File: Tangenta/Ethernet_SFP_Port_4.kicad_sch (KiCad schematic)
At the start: 2 parts, among them J9 HC-SFP-01L

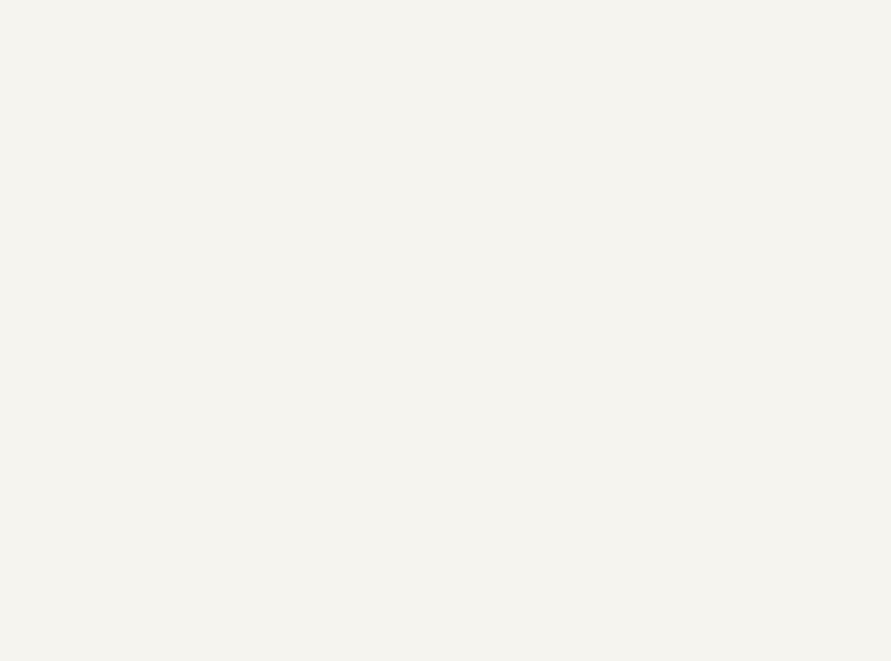
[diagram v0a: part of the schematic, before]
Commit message: Ethernet Switch schematic done, ports TBD...
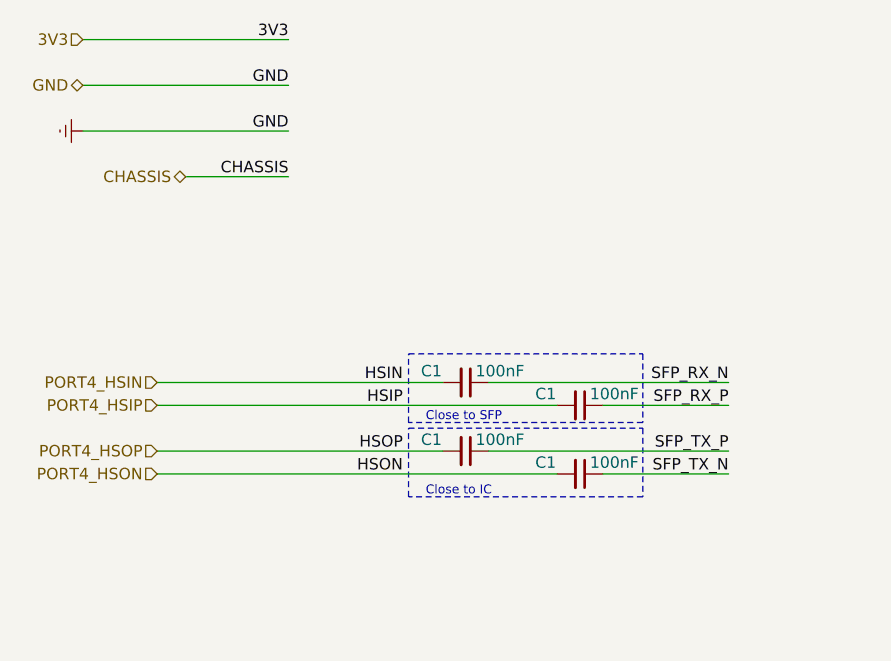
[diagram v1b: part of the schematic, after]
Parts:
- added C1 (x4): 100nF, Capacitor_SMD:C_0402_1005Metric, symbol Device:C_Small
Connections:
- new net PORT4_HSIN: C1.2
- new net PORT4_HSIP: C1.2
- new net PORT4_HSON: C1.2
- new net PORT4_HSOP: C1.2
- new net SFP_RX_N: C1.1
- new net SFP_RX_P: C1.1
- new net SFP_TX_N: C1.1
- new net SFP_TX_P: C1.1
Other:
- note added: "Close to IC"
- note added: "Close to SFP"

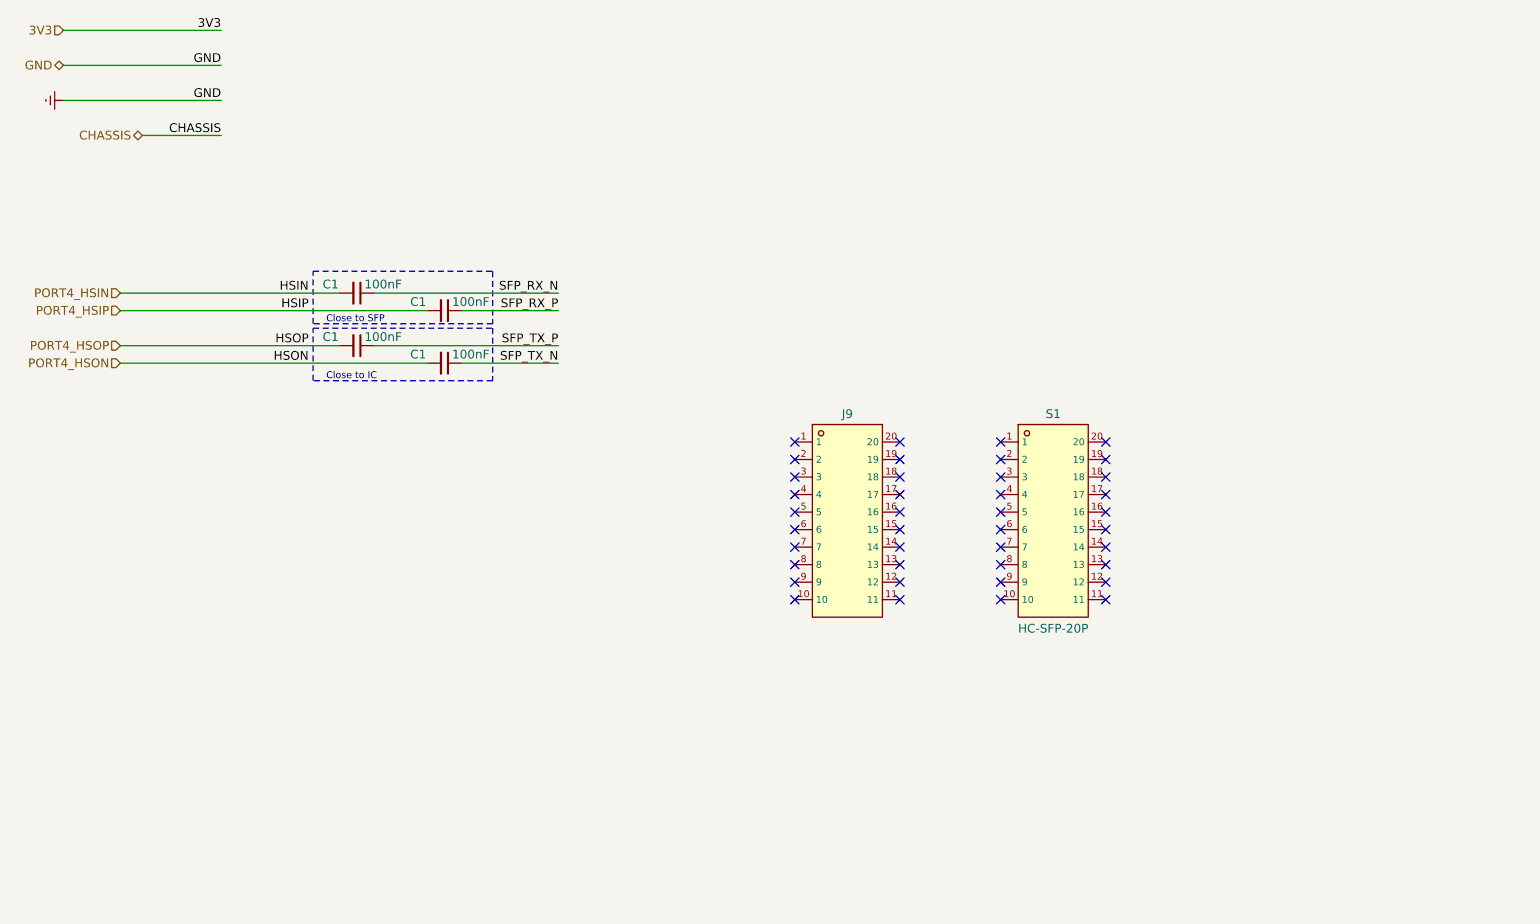
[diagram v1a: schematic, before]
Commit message: Ethernet ready for routing.
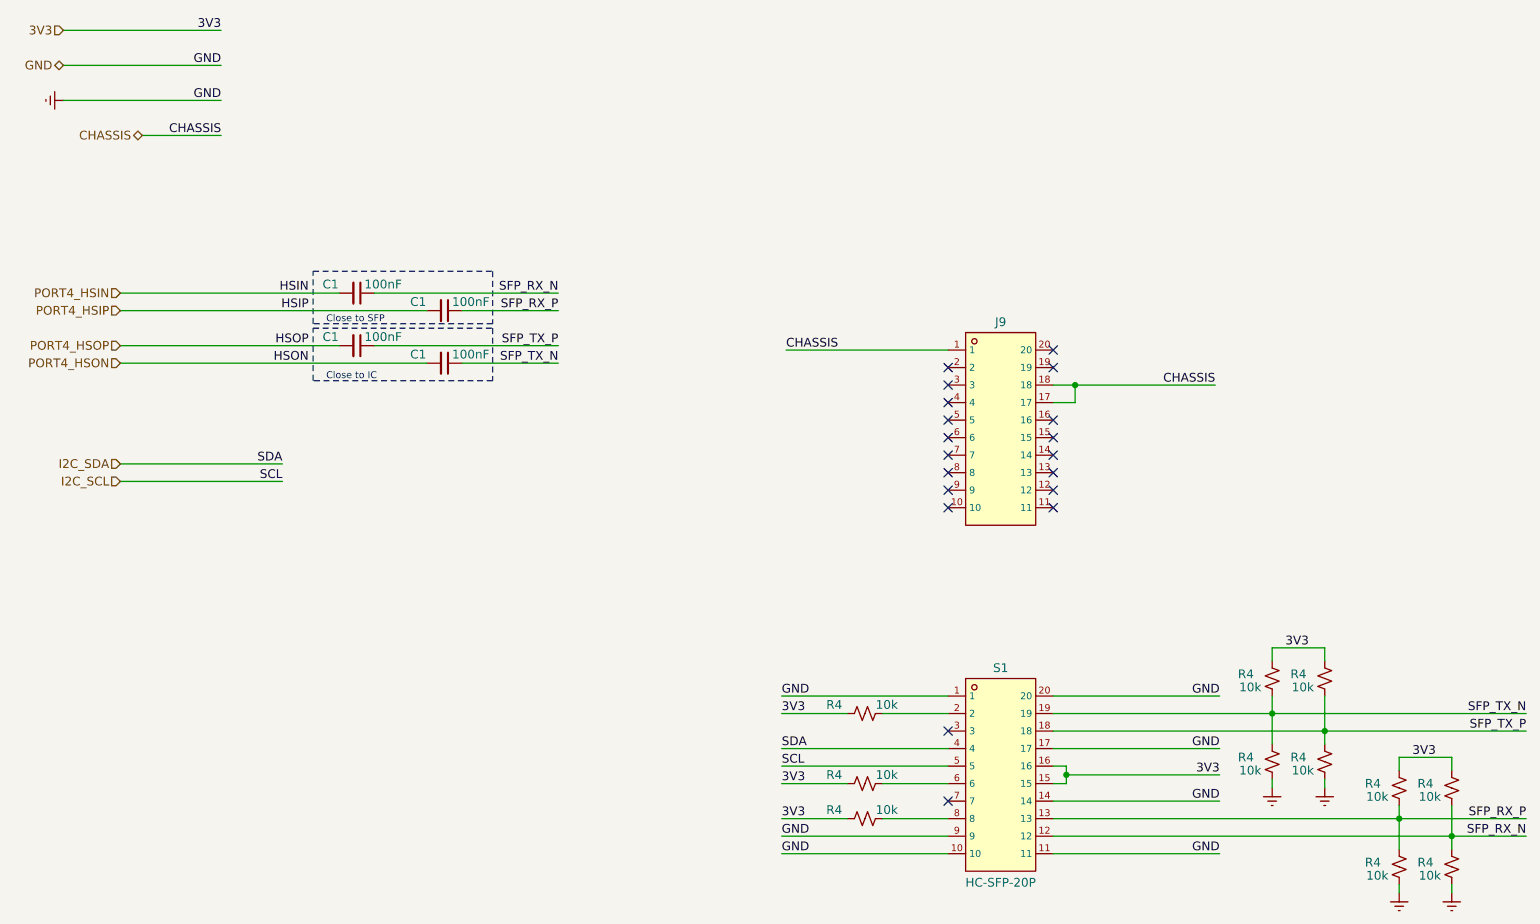
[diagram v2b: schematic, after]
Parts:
- added R4 (x11): 10k, Resistor_SMD:R_0402_1005Metric, symbol Device:R_Small_US
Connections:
- net 3V3: now also S1.15, S1.16, R4.1, R4.1, R4.1, R4.2, R4.2, R4.2, R4.2
- net CHASSIS: now also J9.1, J9.17, J9.18
- net GNDREF: now also S1.1, S1.10, S1.11, S1.14, S1.17, S1.20, S1.9, R4.1, R4.1, R4.1, R4.1
- net SFP_RX_N: now also S1.12, R4.1, R4.2
- net SFP_RX_P: now also S1.13, R4.1, R4.2
- net SFP_TX_N: now also S1.19, R4.1, R4.2
- net SFP_TX_P: now also S1.18, R4.1, R4.2
- net at S1.2: now also R4.2
- net I2C_SDA: now reaches S1.4
- net I2C_SCL: now reaches S1.5
- net at S1.6: now also R4.2
- net at S1.8: now also R4.2
- no-connect marks 40 -> 19
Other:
- moved on the sheet: J9, S1

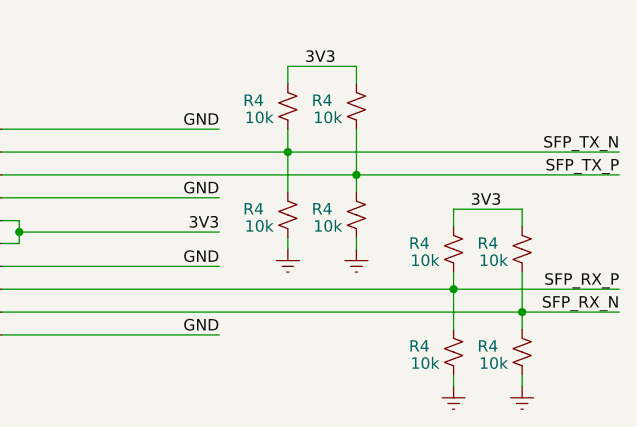
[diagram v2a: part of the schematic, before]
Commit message: Assigned Eth netclasses, MDIO and Toradex connections.
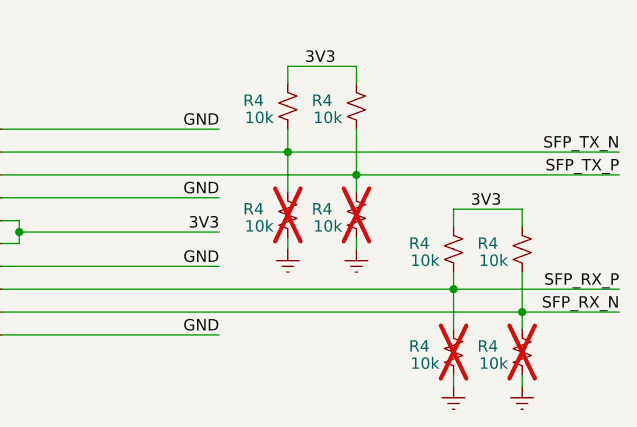
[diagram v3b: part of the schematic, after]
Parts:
- R4: now not fitted; now left out of the parts list
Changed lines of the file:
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@@
   )
   (symbol (lib_id "Device:R_Small_US") (at 217.17 140.335 180) (unit 1)
-    (in_bom yes) (on_board yes) (dnp no)
+    (in_bom no) (on_board yes) (dnp yes)
     (property "Reference" "R4" (at 213.36 139.7 0)
       (effects (font (size 1.27 1.27)))
@@
   )
   (symbol (lib_id "Device:R_Small_US") (at 224.79 140.335 180) (unit 1)
-    (in_bom yes) (on_board yes) (dnp no)
+    (in_bom no) (on_board yes) (dnp yes)
     (property "Reference" "R4" (at 220.98 139.7 0)
       (effects (font (size 1.27 1.27)))
@@
   )
   (symbol (lib_id "Device:R_Small_US") (at 198.755 125.095 180) (unit 1)
-    (in_bom yes) (on_board yes) (dnp no)
+    (in_bom no) (on_board yes) (dnp yes)
     (property "Reference" "R4" (at 194.945 124.46 0)
       (effects (font (size 1.27 1.27)))
@@
   )
   (symbol (lib_id "Device:R_Small_US") (at 206.375 125.095 180) (unit 1)
-    (in_bom yes) (on_board yes) (dnp no)
+    (in_bom no) (on_board yes) (dnp yes)
     (property "Reference" "R4" (at 202.565 124.46 0)
       (effects (font (size 1.27 1.27)))

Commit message: Libraries exported from global to project.
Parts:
- C1: symbol Device:C_Small -> CholaSymbolsPrjLib:C_Small
- J9: symbol SFP_CAGE:HC-SFP-01L -> CholaSymbolsPrjLib:HC-SFP-01L
- R4: symbol Device:R_Small_US -> CholaSymbolsPrjLib:R_Small_US
- S1: symbol SFP_Connector:HC-SFP-20P -> CholaSymbolsPrjLib:HC-SFP-20P
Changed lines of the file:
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@@
     (effects (font (size 1.27 1.27)) (justify right))
   )
-  (symbol (lib_id "Device:C_Small") (at 66.04 64.77 270) (unit 1)
+  (symbol (lib_id "CholaSymbolsPrjLib:C_Small") (at 66.04 64.77 270) (unit 1)
     (in_bom yes) (on_board yes) (dnp no)
     (property "Reference" "C1" (at 62.23 63.5 90)
@@
     )
   )
-  (symbol (lib_id "Device:R_Small_US") (at 224.79 128.905 180) (unit 1)
+  (symbol (lib_id "CholaSymbolsPrjLib:R_Small_US") (at 224.79 128.905 180) (unit 1)
     (in_bom yes) (on_board yes) (dnp no)
     (property "Reference" "R4" (at 220.98 128.27 0)
@@
     )
   )
-  (symbol (lib_id "Device:R_Small_US") (at 139.7 118.11 90) (unit 1)
+  (symbol (lib_id "CholaSymbolsPrjLib:R_Small_US") (at 139.7 118.11 90) (unit 1)
     (in_bom yes) (on_board yes) (dnp no)
     (property "Reference" "R4" (at 135.255 116.84 90)
@@
     )
   )
-  (symbol (lib_id "SFP_CAGE:HC-SFP-01L") (at 159.385 76.835 0) (unit 1)
+  (symbol (lib_id "CholaSymbolsPrjLib:HC-SFP-01L") (at 159.385 76.835 0) (unit 1)
     (in_bom yes) (on_board yes) (dnp no)
     (property "Reference" "J9" (at 159.385 61.341 0)
@@
     )
   )
-  (symbol (lib_id "Device:R_Small_US") (at 217.17 140.335 180) (unit 1)
+  (symbol (lib_id "CholaSymbolsPrjLib:R_Small_US") (at 217.17 140.335 180) (unit 1)
     (in_bom no) (on_board yes) (dnp yes)
     (property "Reference" "R4" (at 213.36 139.7 0)
@@
     )
   )
-  (symbol (lib_id "Device:R_Small_US") (at 139.7 133.35 90) (unit 1)
+  (symbol (lib_id "CholaSymbolsPrjLib:R_Small_US") (at 139.7 133.35 90) (unit 1)
     (in_bom yes) (on_board yes) (dnp no)
     (property "Reference" "R4" (at 135.255 132.08 90)
@@
     )
   )
-  (symbol (lib_id "Device:C_Small") (at 78.74 59.69 270) (unit 1)
+  (symbol (lib_id "CholaSymbolsPrjLib:C_Small") (at 78.74 59.69 270) (unit 1)
     (in_bom yes) (on_board yes) (dnp no)
     (property "Reference" "C1" (at 74.93 58.42 90)
@@
     )
   )
-  (symbol (lib_id "SFP_Connector:HC-SFP-20P") (at 159.385 127 0) (unit 1)
+  (symbol (lib_id "CholaSymbolsPrjLib:HC-SFP-20P") (at 159.385 127 0) (unit 1)
     (in_bom yes) (on_board yes) (dnp no)
     (property "Reference" "S1" (at 159.385 111.506 0)
@@
     )
   )
-  (symbol (lib_id "Device:R_Small_US") (at 217.17 128.905 180) (unit 1)
+  (symbol (lib_id "CholaSymbolsPrjLib:R_Small_US") (at 217.17 128.905 180) (unit 1)
     (in_bom yes) (on_board yes) (dnp no)
     (property "Reference" "R4" (at 213.36 128.27 0)
@@
     )
   )
-  (symbol (lib_id "Device:R_Small_US") (at 198.755 113.03 180) (unit 1)
+  (symbol (lib_id "CholaSymbolsPrjLib:R_Small_US") (at 198.755 113.03 180) (unit 1)
     (in_bom yes) (on_board yes) (dnp no)
     (property "Reference" "R4" (at 194.945 112.395 0)
@@
     )
   )
-  (symbol (lib_id "Device:C_Small") (at 78.74 67.31 270) (unit 1)
+  (symbol (lib_id "CholaSymbolsPrjLib:C_Small") (at 78.74 67.31 270) (unit 1)
     (in_bom yes) (on_board yes) (dnp no)
     (property "Reference" "C1" (at 74.93 66.04 90)
@@
     )
   )
-  (symbol (lib_id "Device:R_Small_US") (at 224.79 140.335 180) (unit 1)
+  (symbol (lib_id "CholaSymbolsPrjLib:R_Small_US") (at 224.79 140.335 180) (unit 1)
     (in_bom no) (on_board yes) (dnp yes)
     (property "Reference" "R4" (at 220.98 139.7 0)
@@
     )
   )
-  (symbol (lib_id "Device:C_Small") (at 66.04 57.15 270) (unit 1)
+  (symbol (lib_id "CholaSymbolsPrjLib:C_Small") (at 66.04 57.15 270) (unit 1)
     (in_bom yes) (on_board yes) (dnp no)
     (property "Reference" "C1" (at 62.23 55.88 90)
@@
     )
   )
-  (symbol (lib_id "Device:R_Small_US") (at 198.755 125.095 180) (unit 1)
+  (symbol (lib_id "CholaSymbolsPrjLib:R_Small_US") (at 198.755 125.095 180) (unit 1)
     (in_bom no) (on_board yes) (dnp yes)
     (property "Reference" "R4" (at 194.945 124.46 0)
@@
     )
   )
-  (symbol (lib_id "Device:R_Small_US") (at 206.375 113.03 180) (unit 1)
+  (symbol (lib_id "CholaSymbolsPrjLib:R_Small_US") (at 206.375 113.03 180) (unit 1)
     (in_bom yes) (on_board yes) (dnp no)
     (property "Reference" "R4" (at 202.565 112.395 0)
@@
     )
   )
-  (symbol (lib_id "Device:R_Small_US") (at 139.7 128.27 90) (unit 1)
+  (symbol (lib_id "CholaSymbolsPrjLib:R_Small_US") (at 139.7 128.27 90) (unit 1)
     (in_bom yes) (on_board yes) (dnp no)
     (property "Reference" "R4" (at 135.255 127 90)
@@
     )
   )
-  (symbol (lib_id "Device:R_Small_US") (at 206.375 125.095 180) (unit 1)
+  (symbol (lib_id "CholaSymbolsPrjLib:R_Small_US") (at 206.375 125.095 180) (unit 1)
     (in_bom no) (on_board yes) (dnp yes)
     (property "Reference" "R4" (at 202.565 124.46 0)

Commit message: ...
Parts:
- C1: symbol CholaSymbolsPrjLib:C_Small -> LocalPrjLib:C_Small
- J9: symbol CholaSymbolsPrjLib:HC-SFP-01L -> LocalPrjLib:HC-SFP-01L
- R4: symbol CholaSymbolsPrjLib:R_Small_US -> LocalPrjLib:R_Small_US
- S1: symbol CholaSymbolsPrjLib:HC-SFP-20P -> LocalPrjLib:HC-SFP-20P
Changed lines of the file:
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@@
     (effects (font (size 1.27 1.27)) (justify right))
   )
-  (symbol (lib_id "CholaSymbolsPrjLib:C_Small") (at 66.04 64.77 270) (unit 1)
+  (symbol (lib_id "LocalPrjLib:C_Small") (at 66.04 64.77 270) (unit 1)
     (in_bom yes) (on_board yes) (dnp no)
     (property "Reference" "C1" (at 62.23 63.5 90)
@@
     )
   )
-  (symbol (lib_id "CholaSymbolsPrjLib:R_Small_US") (at 224.79 128.905 180) (unit 1)
+  (symbol (lib_id "LocalPrjLib:R_Small_US") (at 224.79 128.905 180) (unit 1)
     (in_bom yes) (on_board yes) (dnp no)
     (property "Reference" "R4" (at 220.98 128.27 0)
@@
     )
   )
-  (symbol (lib_id "CholaSymbolsPrjLib:R_Small_US") (at 139.7 118.11 90) (unit 1)
+  (symbol (lib_id "LocalPrjLib:R_Small_US") (at 139.7 118.11 90) (unit 1)
     (in_bom yes) (on_board yes) (dnp no)
     (property "Reference" "R4" (at 135.255 116.84 90)
@@
     )
   )
-  (symbol (lib_id "CholaSymbolsPrjLib:HC-SFP-01L") (at 159.385 76.835 0) (unit 1)
+  (symbol (lib_id "LocalPrjLib:HC-SFP-01L") (at 159.385 76.835 0) (unit 1)
     (in_bom yes) (on_board yes) (dnp no)
     (property "Reference" "J9" (at 159.385 61.341 0)
@@
     )
   )
-  (symbol (lib_id "CholaSymbolsPrjLib:R_Small_US") (at 217.17 140.335 180) (unit 1)
+  (symbol (lib_id "LocalPrjLib:R_Small_US") (at 217.17 140.335 180) (unit 1)
     (in_bom no) (on_board yes) (dnp yes)
     (property "Reference" "R4" (at 213.36 139.7 0)
@@
     )
   )
-  (symbol (lib_id "CholaSymbolsPrjLib:R_Small_US") (at 139.7 133.35 90) (unit 1)
+  (symbol (lib_id "LocalPrjLib:R_Small_US") (at 139.7 133.35 90) (unit 1)
     (in_bom yes) (on_board yes) (dnp no)
     (property "Reference" "R4" (at 135.255 132.08 90)
@@
     )
   )
-  (symbol (lib_id "CholaSymbolsPrjLib:C_Small") (at 78.74 59.69 270) (unit 1)
+  (symbol (lib_id "LocalPrjLib:C_Small") (at 78.74 59.69 270) (unit 1)
     (in_bom yes) (on_board yes) (dnp no)
     (property "Reference" "C1" (at 74.93 58.42 90)
@@
     )
   )
-  (symbol (lib_id "CholaSymbolsPrjLib:HC-SFP-20P") (at 159.385 127 0) (unit 1)
+  (symbol (lib_id "LocalPrjLib:HC-SFP-20P") (at 159.385 127 0) (unit 1)
     (in_bom yes) (on_board yes) (dnp no)
     (property "Reference" "S1" (at 159.385 111.506 0)
@@
     )
   )
-  (symbol (lib_id "CholaSymbolsPrjLib:R_Small_US") (at 217.17 128.905 180) (unit 1)
+  (symbol (lib_id "LocalPrjLib:R_Small_US") (at 217.17 128.905 180) (unit 1)
     (in_bom yes) (on_board yes) (dnp no)
     (property "Reference" "R4" (at 213.36 128.27 0)
@@
     )
   )
-  (symbol (lib_id "CholaSymbolsPrjLib:R_Small_US") (at 198.755 113.03 180) (unit 1)
+  (symbol (lib_id "LocalPrjLib:R_Small_US") (at 198.755 113.03 180) (unit 1)
     (in_bom yes) (on_board yes) (dnp no)
     (property "Reference" "R4" (at 194.945 112.395 0)
@@
     )
   )
-  (symbol (lib_id "CholaSymbolsPrjLib:C_Small") (at 78.74 67.31 270) (unit 1)
+  (symbol (lib_id "LocalPrjLib:C_Small") (at 78.74 67.31 270) (unit 1)
     (in_bom yes) (on_board yes) (dnp no)
     (property "Reference" "C1" (at 74.93 66.04 90)
@@
     )
   )
-  (symbol (lib_id "CholaSymbolsPrjLib:R_Small_US") (at 224.79 140.335 180) (unit 1)
+  (symbol (lib_id "LocalPrjLib:R_Small_US") (at 224.79 140.335 180) (unit 1)
     (in_bom no) (on_board yes) (dnp yes)
     (property "Reference" "R4" (at 220.98 139.7 0)
@@
     )
   )
-  (symbol (lib_id "CholaSymbolsPrjLib:C_Small") (at 66.04 57.15 270) (unit 1)
+  (symbol (lib_id "LocalPrjLib:C_Small") (at 66.04 57.15 270) (unit 1)
     (in_bom yes) (on_board yes) (dnp no)
     (property "Reference" "C1" (at 62.23 55.88 90)
@@
     )
   )
-  (symbol (lib_id "CholaSymbolsPrjLib:R_Small_US") (at 198.755 125.095 180) (unit 1)
+  (symbol (lib_id "LocalPrjLib:R_Small_US") (at 198.755 125.095 180) (unit 1)
     (in_bom no) (on_board yes) (dnp yes)
     (property "Reference" "R4" (at 194.945 124.46 0)
@@
     )
   )
-  (symbol (lib_id "CholaSymbolsPrjLib:R_Small_US") (at 206.375 113.03 180) (unit 1)
+  (symbol (lib_id "LocalPrjLib:R_Small_US") (at 206.375 113.03 180) (unit 1)
     (in_bom yes) (on_board yes) (dnp no)
     (property "Reference" "R4" (at 202.565 112.395 0)
@@
     )
   )
-  (symbol (lib_id "CholaSymbolsPrjLib:R_Small_US") (at 139.7 128.27 90) (unit 1)
+  (symbol (lib_id "LocalPrjLib:R_Small_US") (at 139.7 128.27 90) (unit 1)
     (in_bom yes) (on_board yes) (dnp no)
     (property "Reference" "R4" (at 135.255 127 90)
@@
     )
   )
-  (symbol (lib_id "CholaSymbolsPrjLib:R_Small_US") (at 206.375 125.095 180) (unit 1)
+  (symbol (lib_id "LocalPrjLib:R_Small_US") (at 206.375 125.095 180) (unit 1)
     (in_bom no) (on_board yes) (dnp yes)
     (property "Reference" "R4" (at 202.565 124.46 0)
